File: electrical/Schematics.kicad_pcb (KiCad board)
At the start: 2 copper layers, 85.5 x 65 mm, 24 parts, among them J1 12V_IN, J2 RGB_STRIP_1, J3 WHITE_STRIP_1, J4 WHITE_STRIP_2, J5 RGB_STRIP_2, Q1 IRLB8721PBF, Q2 2N7000, Q3 IRLB8721PBF, Q4 2N7000, SW1 BTN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

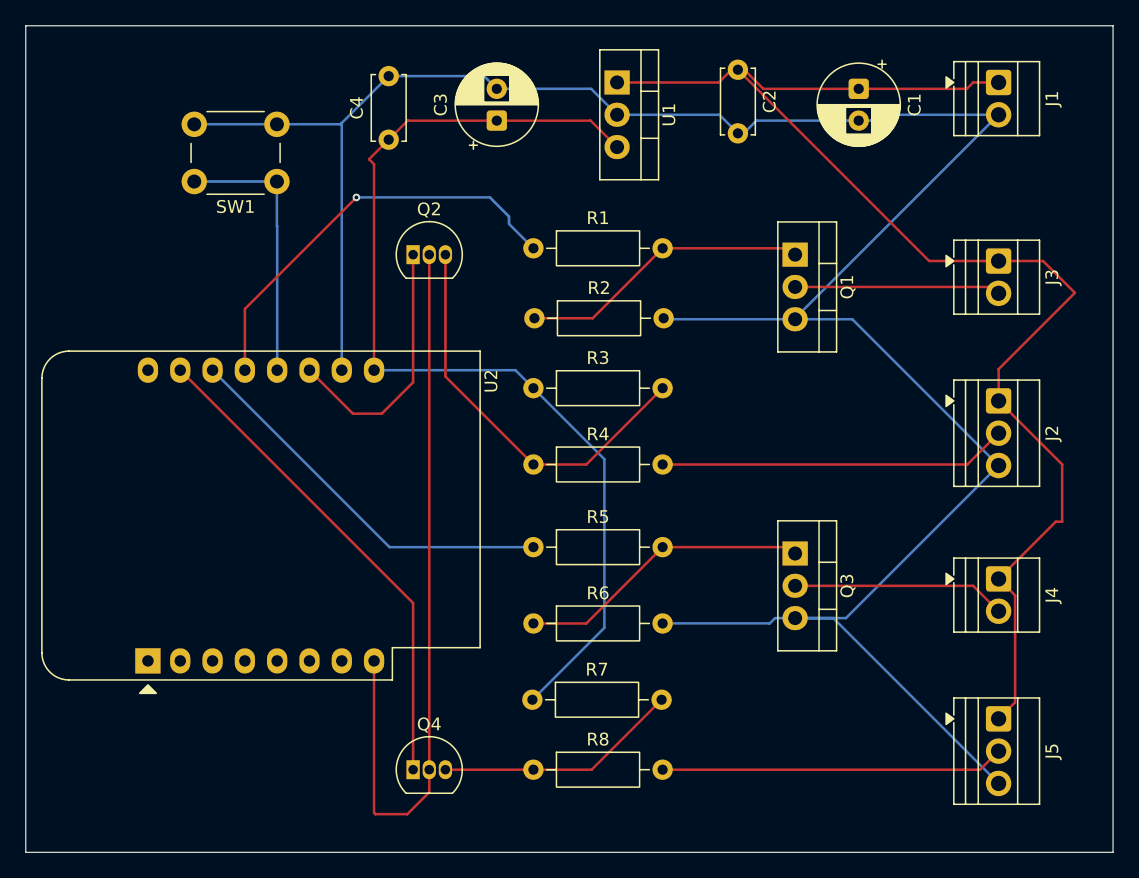
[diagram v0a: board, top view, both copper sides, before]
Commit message: changed design to fit the ordered esp module
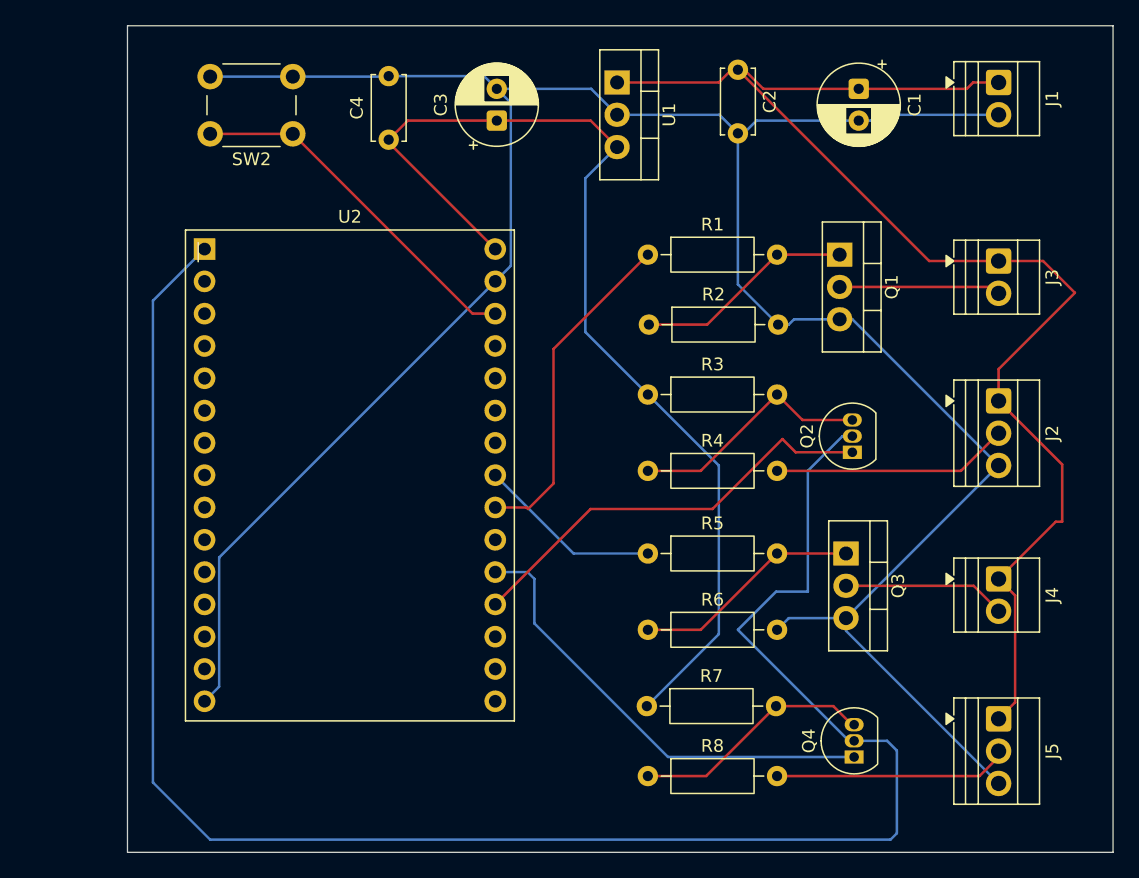
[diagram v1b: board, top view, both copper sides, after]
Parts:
- removed SW1: BTN, Button_Switch_THT:SW_PUSH_6mm
- added SW2: BTN, Button_Switch_THT:SW_PUSH_6mm, F.Cu at (136.0, 66.0)
- U2: value WEMOS_D1_mini -> NodeMCU-ESP32-30pin; footprint RF_Module:WEMOS_D1_mini_light -> WideRangeLEDLamp:NodeMCU-ESP32-30pin
- moved Q2 37.9 mm to (180.0, 91.0), turned to 90 degrees
- moved Q4 34.7 mm to (180.1, 115.0), turned to 90 degrees
- moved U2 32.7 mm to (129.1, 75.1), turned to 0 degrees
- moved R1 9.01 mm to (163.9, 75.5)
- moved R2 9.01 mm to (164.0, 81.0)
- moved R3 9.01 mm to (163.9, 86.5)
- moved R4 9.01 mm to (163.9, 92.5)
- moved R5 9.01 mm to (163.9, 99.0)
- moved R6 9.01 mm to (163.9, 105.0)
- moved R7 9.01 mm to (163.8, 111.0)
- moved R8 9.01 mm to (163.9, 116.5)
- moved Q3 4.00 mm to (179.5, 99.0)
- moved Q1 3.50 mm to (179.0, 75.5)
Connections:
- U2 pad 1: unconnected-(U2-~{RST}-Pad1) -> /+3V3
- U2 pad 10: /GND -> unconnected-(U2-IO26-Pad10)
- U2 pad 11: /RGB_DATA_1 -> unconnected-(U2-IO27-Pad11)
- U2 pad 12: Net-(U2-D3) -> unconnected-(U2-IO14-Pad12)
- U2 pad 13: /WHITE_PWM_1 -> unconnected-(U2-IO12-Pad13)
- U2 pad 14: /WHITE_PWM_2 -> unconnected-(U2-IO13-Pad14)
- U2 pad 15: /RGB_DATA_2 -> /GND
- U2 pad 16: unconnected-(U2-TX-Pad16) -> /+5V
- U2 pad 8: /+3V3 -> unconnected-(U2-IO33-Pad8)
- U2 pad 9: /+5V -> unconnected-(U2-IO25-Pad9)
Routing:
- net /+3V3: track 59.3 -> 148.6 mm
- net Net-(U2-IO23): track 0.00 -> 28.3 mm
- net Net-(U2-D3): track 21.3 -> 0.00 mm
- net /WHITE_PWM_2: track 31.0 -> 14.6 mm
- net /RGB_DATA_1: track 20.6 -> 33.9 mm
- net Net-(Q2-D): track 32.0 -> 19.4 mm
- net Net-(J2-Pin_2): track 27.4 -> 18.6 mm
- net Net-(J5-Pin_2): track 27.0 -> 18.5 mm
- net /GND: track 195.9 -> 204.4 mm
- net /WHITE_PWM_1: track 33.1 -> 26.5 mm, vias 1 -> 0
- net Net-(Q1-G): track 23.0 -> 17.3 mm
- net Net-(Q3-G): track 23.3 -> 18.1 mm
- net Net-(J4-Pin_2): track 16.8 -> 12.9 mm
- net Net-(J3-Pin_2): track 16.2 -> 12.7 mm
- net /RGB_DATA_2: track 39.0 -> 36.3 mm
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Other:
- board size 85.5 x 65 mm -> 77.5 x 65 mm

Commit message: changes according to actual build
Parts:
- removed Q2, Q4: 2N7000, Package_TO_SOT_THT:TO-92_Inline
- removed R3, R7: R4K7, Resistor_THT:R_Axial_DIN0207_L6.3mm_D2.5mm_P10.16mm_Horizontal
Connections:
- R4 pad 1: Net-(Q2-D) -> /RGB_DATA_1
- R8 pad 1: Net-(Q4-D) -> /RGB_DATA_2
- U2 pad 1: /+3V3 -> unconnected-(U2-3V3-Pad1)
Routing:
- net /+3V3: track 148.6 -> 0.00 mm
- net /+5V: track 83.8 -> 32.1 mm
- net Net-(Q2-D): track 19.4 -> 0.00 mm
- net Net-(Q4-D): track 19.1 -> 0.00 mm
- net /RGB_DATA_1: track 33.9 -> 16.3 mm
- net /RGB_DATA_2: track 36.3 -> 21.0 mm
